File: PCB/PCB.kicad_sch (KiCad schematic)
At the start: 35 parts, among them J1 USB_C_Receptacle_USB2.0_16P, SW1 SW_Push, SW2 SW_Push, U1 RP2040, U2 USBLC6-2SC6, U3 NCP1117ST33T3G, U4 W25Q32JVSS, U5 Conn, Y1 Crystal_GND24

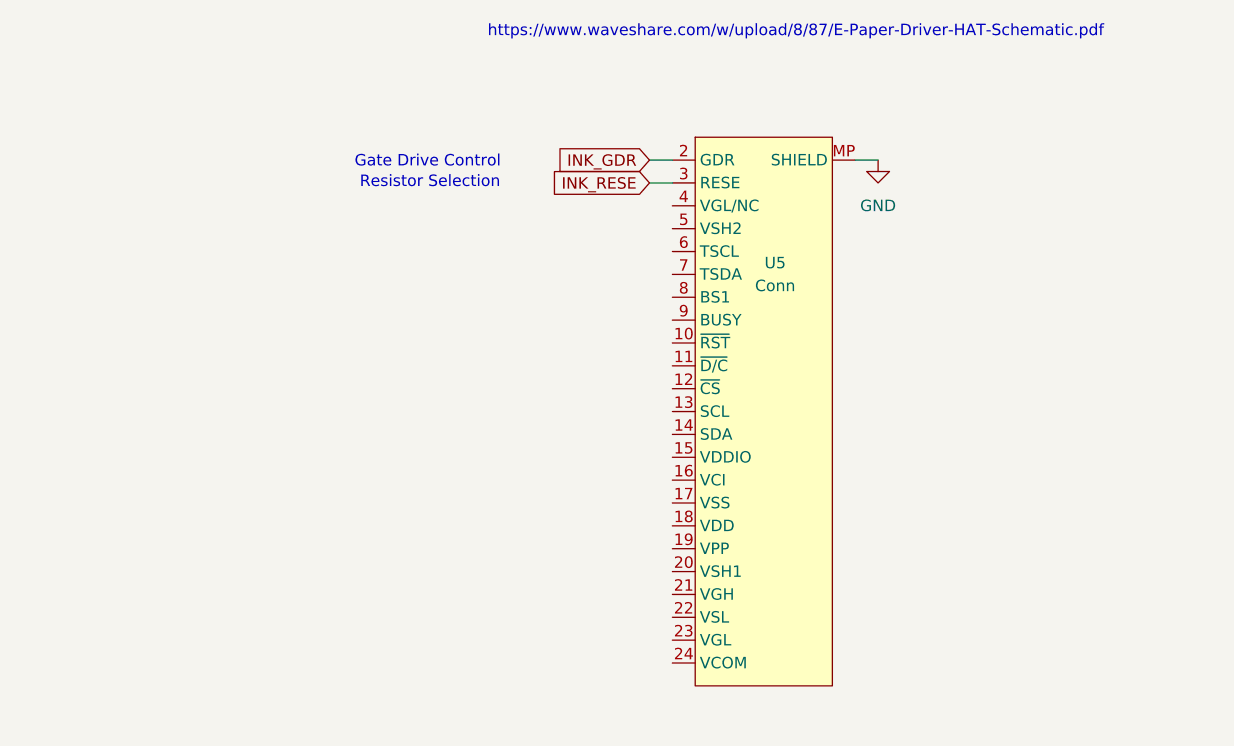
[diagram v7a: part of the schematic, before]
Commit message: more eink wiring
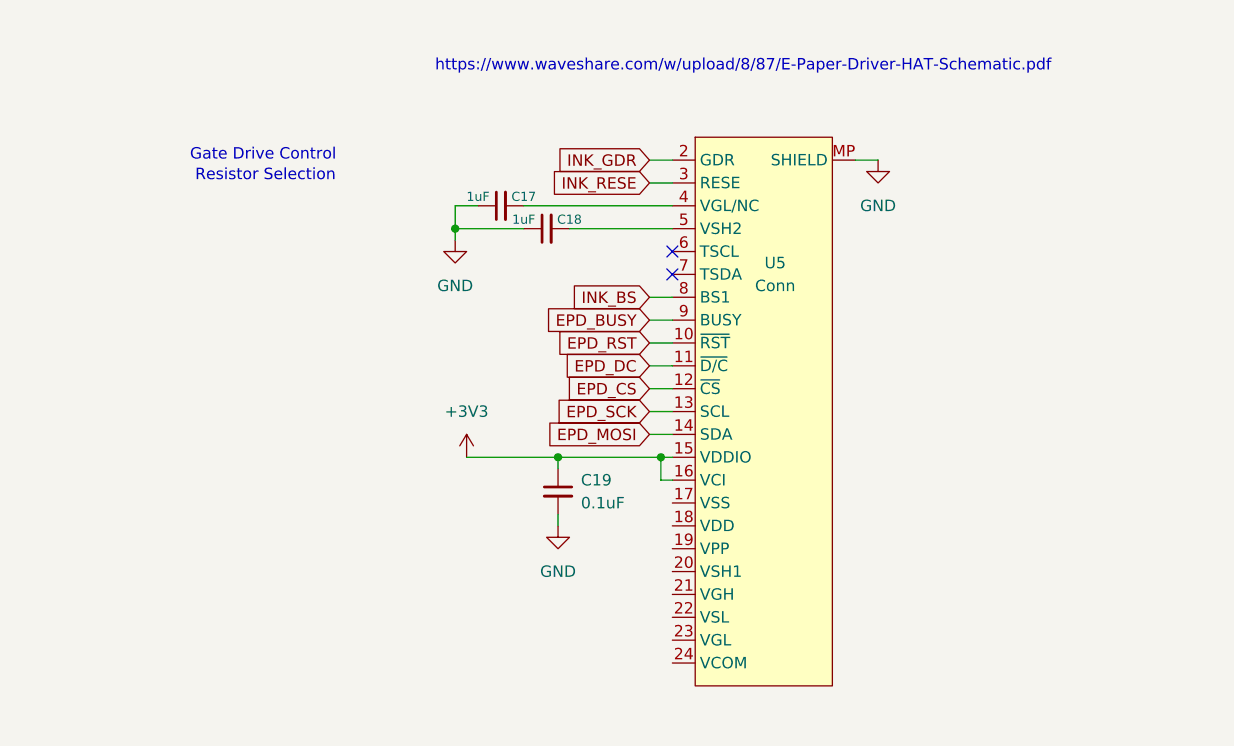
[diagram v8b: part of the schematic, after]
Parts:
- added C17, C18: 1uF, symbol Device:C_Small
- added C19: 0.1uF, symbol Device:C_Small
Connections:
- net +3V3: now also U5.15 (VDDIO), U5.16 (VCI), C19.1
- net GND: now also C17.1, C18.1, C19.2
- net EPD_RST: now reaches U5.10 (~{RST})
- net EPD_DC: now reaches U5.11 (~{D/C})
- net EPD_CS: now reaches U5.12 (~{CS})
- net EPD_SCK: now reaches U5.13 (SCL)
- net EPD_MOSI: now reaches U5.14 (SDA)
- net at U5.4 (VGL/NC): now also C17.2
- net at U5.5 (VSH2): now also C18.2
- net INK_BS: now reaches U5.8 (BS1)
- net EPD_BUSY: now reaches U5.9 (BUSY)
- no-connect marks 2 -> 4
